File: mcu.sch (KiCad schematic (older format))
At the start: 0 parts

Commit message: Praca nad sch, dodana sekcja zasilania i karta sd
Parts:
- added C? (x6): 100n, symbol Device:C
- added C? (x4): C, symbol Device:C
- added FB?: Ferrite_Bead_Small, symbol Device:Ferrite_Bead_Small
- added J?: Micro_SD_Card, symbol Connector:Micro_SD_Card
- added R? (x5): 50k, symbol Device:R
- added U?: STM32F042K6Tx, Package_QFP:LQFP-32_7x7mm_P0.8mm, symbol MCU_ST_STM32F0:STM32F042K6Tx
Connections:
- new net: J?.1 (DAT2), R?.2
- new net: J?.8 (DAT1), R?.1
- new net +3.3VA: C?.1, C?.1, C?.1, C?.1, FB?.2, U?.5 (VDDA)
- new net +3V3: C?.1, C?.1, C?.2, C?.2, C?.2, C?.2, FB?.1, J?.4 (VDD), R?.1, R?.1, R?.1, R?.1, R?.2, U?.1 (VDD), U?.17 (VDDIO2)
- new net GND: C?.1, C?.1, C?.1, C?.1, C?.2, C?.2, J?.6 (VSS), J?.9 (SHIELD), U?.16 (VSS)
- new net GNDA: C?.2, C?.2, C?.2, C?.2, U?.32 (VSSA)
- new net SDCLK: J?.5 (CLK)
- new net SDMISO: J?.7 (DAT0), R?.2
- new net SDMOSI: J?.3 (CMD), R?.2
- new net SD~SS: J?.2 (DAT3/CD), R?.2

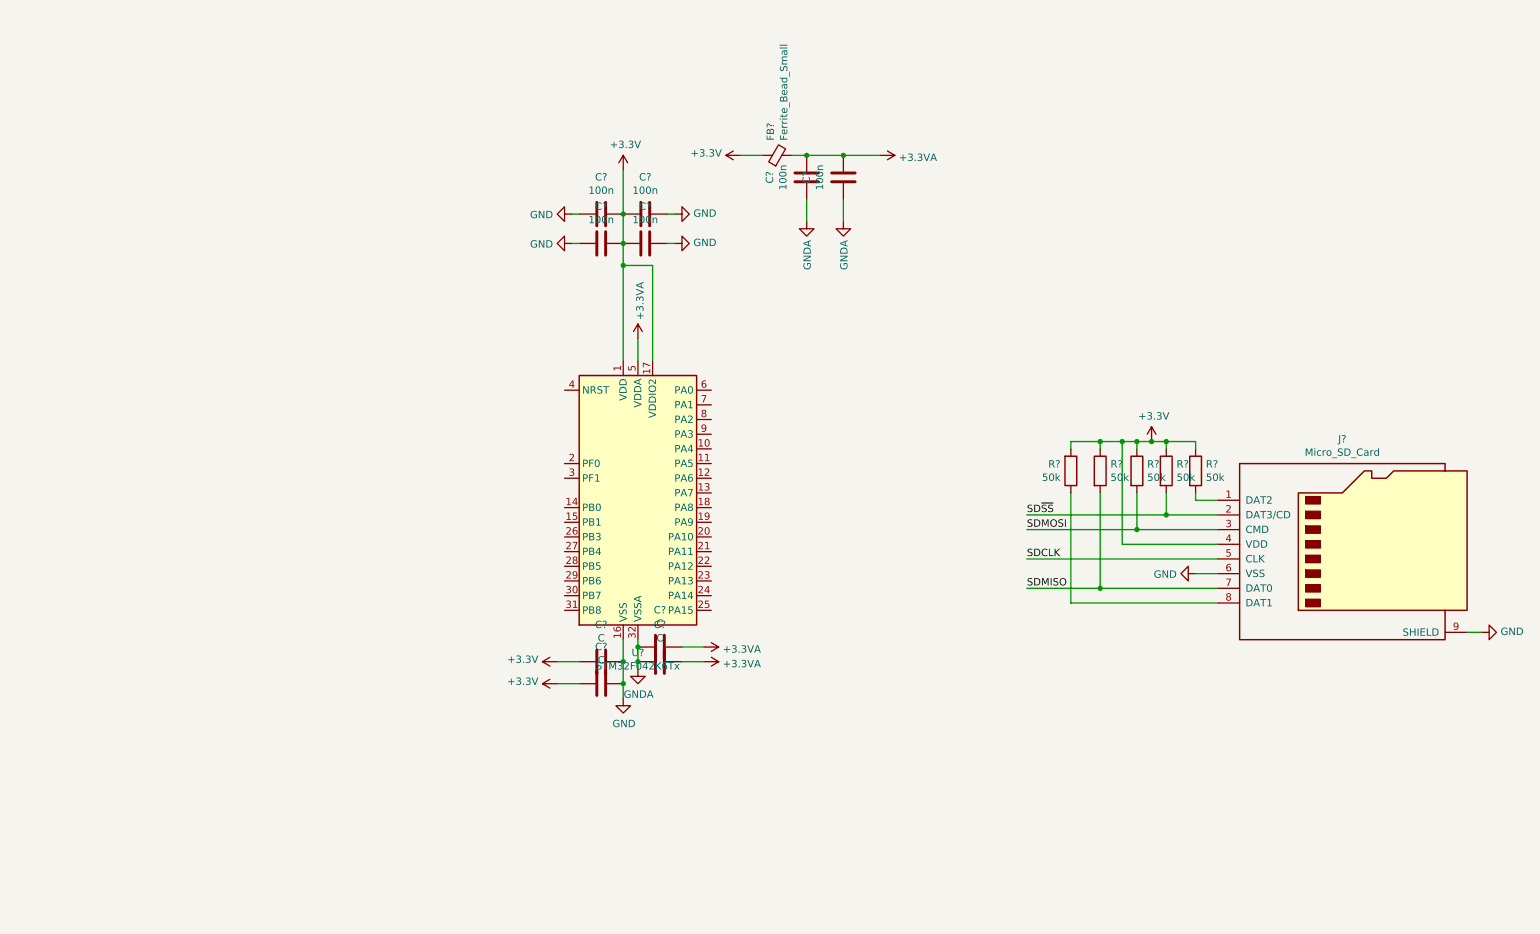
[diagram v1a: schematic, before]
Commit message: dalsza praca nad sch, przypisanie pinów
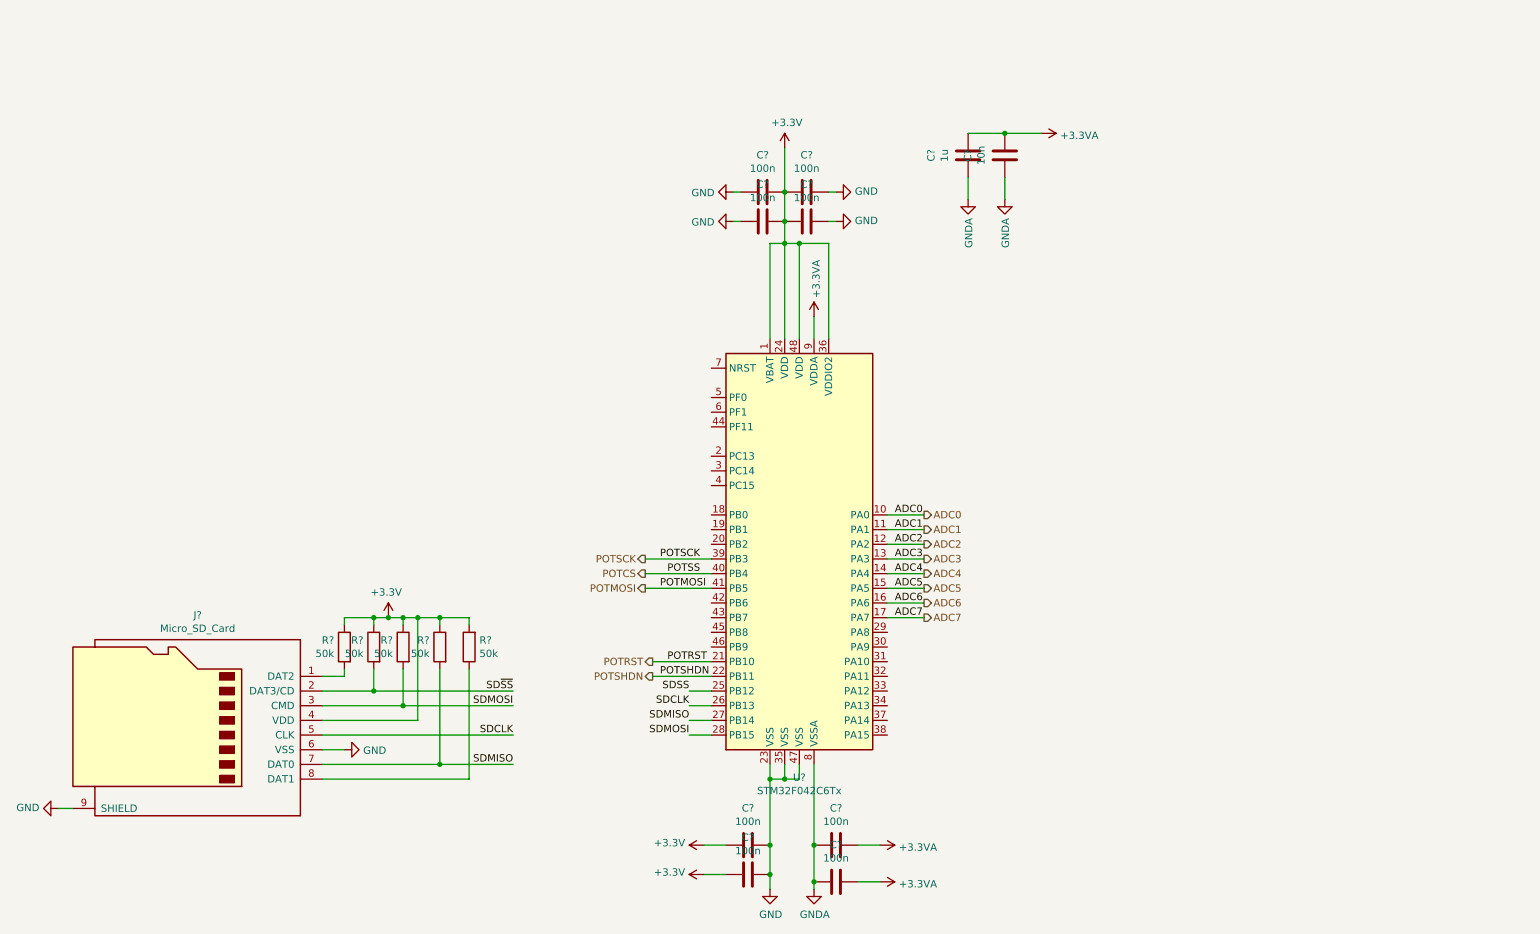
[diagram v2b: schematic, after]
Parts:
- removed C? (x3): C, symbol Device:C
- removed FB?: Ferrite_Bead_Small, symbol Device:Ferrite_Bead_Small
- removed U?: STM32F042K6Tx, Package_QFP:LQFP-32_7x7mm_P0.8mm, symbol MCU_ST_STM32F0:STM32F042K6Tx
- added C? (x3): 100n, symbol Device:C
- added U?: STM32F042C6Tx, Package_QFP:LQFP-48_7x7mm_P0.5mm, symbol MCU_ST_STM32F0:STM32F042C6Tx
- C?: value 100n -> 1u
- C?: value C -> 100n
- C?: value 100n -> 10n
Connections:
- net +3.3VA: now also C?.1, C?.1, U?.9 (VDDA)
- net +3V3: now also C?.2, U?.1 (VBAT), U?.24 (VDD), U?.36 (VDDIO2), U?.48 (VDD)
- net GND: now also C?.1, U?.23 (VSS), U?.35 (VSS), U?.47 (VSS)
- net GNDA: now also C?.2, C?.2, U?.8 (VSSA)
- net SDCLK: now also U?.26 (PB13)
- net SDMISO: now also U?.27 (PB14)
- net SDMOSI: now also U?.28 (PB15)
- new net ADC0: U?.10 (PA0)
- new net ADC1: U?.11 (PA1)
- new net ADC2: U?.12 (PA2)
- new net ADC3: U?.13 (PA3)
- new net ADC4: U?.14 (PA4)
- new net ADC5: U?.15 (PA5)
- new net ADC6: U?.16 (PA6)
- new net ADC7: U?.17 (PA7)
- new net POTCS: U?.40 (PB4)
- new net POTMOSI: U?.41 (PB5)
- new net POTRST: U?.21 (PB10)
- new net POTSCK: U?.39 (PB3)
- new net POTSHDN: U?.22 (PB11)
- new net SDSS: U?.25 (PB12)
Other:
- moved on the sheet: C?, J?, R?
